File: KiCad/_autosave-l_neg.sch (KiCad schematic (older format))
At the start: 14 parts, among them Q16 S9013, Q17 S9012, Q18 S9013, SW2 SW_Push_LED

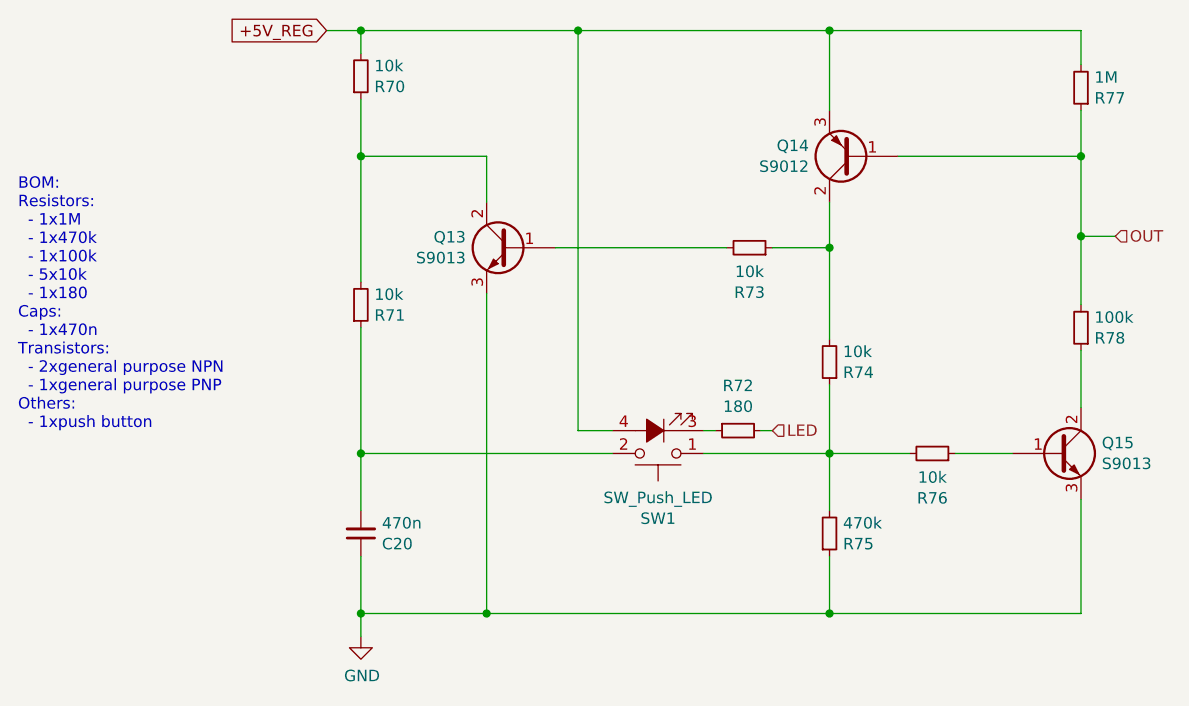
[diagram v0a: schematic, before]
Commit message: finished PCB with TL12
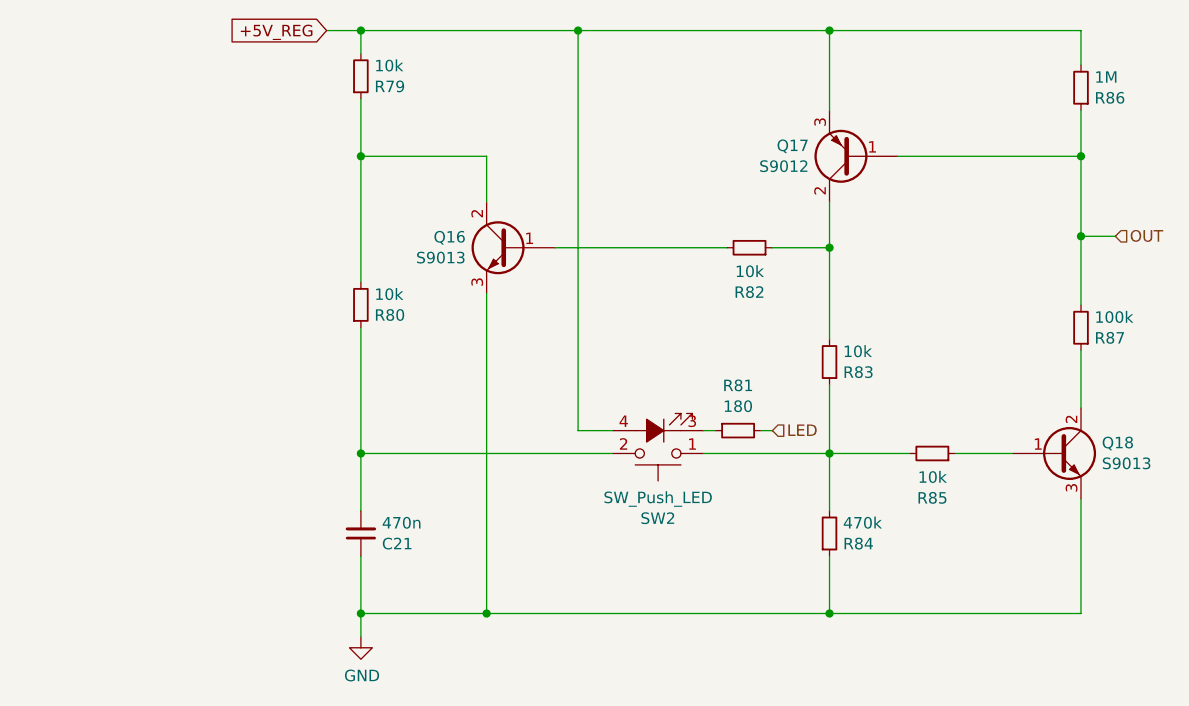
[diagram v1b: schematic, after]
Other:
- note removed: "BOM:\nResistors:\n - 1x1M\n - 1x470k\n - 1x100k\n - 5x10k\n - 1x180\nCaps:\n - 1x470n\nTransistors:\n - 2xgeneral purpose NPN\n - 1xgeneral purpose PNP\nOthers:\n - 1xpush button"
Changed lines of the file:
@@
 $Descr A4 11693 8268
 encoding utf-8
-Sheet 4 4
+Sheet 3 4
 Title ""
 Date ""
@@
 AR Path="/60AC1B12/605CA6A1" Ref="R80"  Part="1"
 AR Path="/60AC1B1E/605CA6A1" Ref="R71"  Part="1"
-F 0 "R71" H 4459 3946 50  0000 L CNN
+F 0 "R80" H 4459 3946 50  0000 L CNN
 F 1 "10k" H 4459 3855 50  0000 L CNN
 F 2 "" H 4400 3900 50  0001 C CNN
@@
 AR Path="/60AC1B12/605D57B8" Ref="C21"  Part="1"
 AR Path="/60AC1B1E/605D57B8" Ref="C20"  Part="1"
-F 0 "C20" H 4492 4946 50  0000 L CNN
+F 0 "C21" H 4492 4946 50  0000 L CNN
 F 1 "470n" H 4492 4855 50  0000 L CNN
 F 2 "" H 4400 4900 50  0001 C CNN
@@
 AR Path="/60AC1B12/605D5FB7" Ref="SW2"  Part="1"
 AR Path="/60AC1B1E/605D5FB7" Ref="SW1"  Part="1"
-F 0 "SW1" H 5700 4835 50  0000 C CNN
+F 0 "SW2" H 5700 4835 50  0000 C CNN
 F 1 "SW_Push_LED" H 5700 4744 50  0000 C CNN
 F 2 "" H 5700 4750 50  0001 C CNN
@@
 AR Path="/60AC1B12/605D8BBC" Ref="R79"  Part="1"
 AR Path="/60AC1B1E/605D8BBC" Ref="R70"  Part="1"
-F 0 "R70" H 4459 2946 50  0000 L CNN
+F 0 "R79" H 4459 2946 50  0000 L CNN
 F 1 "10k" H 4459 2855 50  0000 L CNN
 F 2 "" H 4400 2900 50  0001 C CNN
@@
 AR Path="/60AC1B12/605D9138" Ref="#PWR033"  Part="1"
 AR Path="/60AC1B1E/605D9138" Ref="#PWR032"  Part="1"
-F 0 "#PWR032" H 4400 5100 50  0001 C CNN
+F 0 "#PWR033" H 4400 5100 50  0001 C CNN
 F 1 "GND" H 4405 5177 50  0000 C CNN
 F 2 "" H 4400 5350 50  0001 C CNN
@@
 AR Path="/60AC1B12/605D988B" Ref="R82"  Part="1"
 AR Path="/60AC1B1E/605D988B" Ref="R73"  Part="1"
-F 0 "R73" V 5904 3650 50  0000 C CNN
+F 0 "R82" V 5904 3650 50  0000 C CNN
 F 1 "10k" V 5995 3650 50  0000 C CNN
 F 2 "" H 6100 3650 50  0001 C CNN
@@
 AR Path="/60AC1B12/605DA2A0" Ref="R83"  Part="1"
 AR Path="/60AC1B1E/605DA2A0" Ref="R74"  Part="1"
-F 0 "R74" H 6391 4196 50  0000 R CNN
+F 0 "R83" H 6391 4196 50  0000 R CNN
 F 1 "10k" H 6391 4105 50  0000 R CNN
 F 2 "" H 6450 4150 50  0001 C CNN
@@
 AR Path="/60AC1B12/605DAF7B" Ref="R84"  Part="1"
 AR Path="/60AC1B1E/605DAF7B" Ref="R75"  Part="1"
-F 0 "R75" H 6509 4946 50  0000 L CNN
+F 0 "R84" H 6509 4946 50  0000 L CNN
 F 1 "470k" H 6509 4855 50  0000 L CNN
 F 2 "" H 6450 4900 50  0001 C CNN
@@
 AR Path="/60AC1B12/605DB9E1" Ref="R85"  Part="1"
 AR Path="/60AC1B1E/605DB9E1" Ref="R76"  Part="1"
-F 0 "R76" V 6704 4550 50  0000 C CNN
+F 0 "R85" V 6704 4550 50  0000 C CNN
 F 1 "10k" V 6795 4550 50  0000 C CNN
 F 2 "" H 6900 4550 50  0001 C CNN
@@
 AR Path="/60AC1B12/605DDA9F" Ref="R87"  Part="1"
 AR Path="/60AC1B1E/605DDA9F" Ref="R78"  Part="1"
-F 0 "R78" H 7491 4046 50  0000 R CNN
+F 0 "R87" H 7491 4046 50  0000 R CNN
 F 1 "100k" H 7491 3955 50  0000 R CNN
 F 2 "" H 7550 4000 50  0001 C CNN
@@
 AR Path="/60AC1B12/605DF842" Ref="R86"  Part="1"
 AR Path="/60AC1B1E/605DF842" Ref="R77"  Part="1"
-F 0 "R77" H 7491 2996 50  0000 R CNN
+F 0 "R86" H 7491 2996 50  0000 R CNN
 F 1 "1M" H 7491 2905 50  0000 R CNN
 F 2 "" H 7550 2950 50  0001 C CNN
@@
 AR Path="/60AC1B12/605E2C4C" Ref="R81"  Part="1"
 AR Path="/60AC1B1E/605E2C4C" Ref="R72"  Part="1"
-F 0 "R72" V 5854 4450 50  0000 C CNN
+F 0 "R81" V 5854 4450 50  0000 C CNN
 F 1 "180" V 5945 4450 50  0000 C CNN
 F 2 "" H 6050 4450 50  0001 C CNN
@@
 AR Path="/60AC1B12/60669235" Ref="Q16"  Part="1"
 AR Path="/60AC1B1E/60669235" Ref="Q13"  Part="1"
-F 0 "Q13" H 5241 3696 50  0000 L CNN
+F 0 "Q16" H 5241 3696 50  0000 L CNN
 F 1 "S9013" H 5241 3605 50  0000 L CNN
 F 2 "" H 5250 3750 50  0001 C CNN
@@
 AR Path="/60AC1B12/605DC332" Ref="Q17"  Part="1"
 AR Path="/60AC1B1E/605DC332" Ref="Q14"  Part="1"
-F 0 "Q14" H 6740 3204 50  0000 L CNN
+F 0 "Q17" H 6740 3204 50  0000 L CNN
 F 1 "S9012" H 6740 3295 50  0000 L CNN
 F 2 "" H 6750 3350 50  0001 C CNN
@@
 AR Path="/60AC1B12/6066A306" Ref="Q18"  Part="1"
 AR Path="/60AC1B1E/6066A306" Ref="Q15"  Part="1"
-F 0 "Q15" H 7641 4596 50  0000 L CNN
+F 0 "Q18" H 7641 4596 50  0000 L CNN
 F 1 "S9013" H 7641 4505 50  0000 L CNN
 F 2 "" H 7650 4650 50  0001 C CNN
@@
 Text GLabel 4250 2700 0    50   Input ~ 0
 +5V_REG
-Text Notes 2900 4450 0    50   ~ 0
-BOM:\nResistors:\n  - 1x1M\n  - 1x470k\n  - 1x100k\n  - 5x10k\n  - 1x180\nCaps:\n  - 1x470n\nTransistors:\n  - 2xgeneral purpose NPN\n  - 1xgeneral purpose PNP\nOthers:\n  - 1xpush button
 $EndSCHEMATC
